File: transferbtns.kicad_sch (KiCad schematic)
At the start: 23 parts, among them J17 8P8C, J18 8P8C, U6 74LS165

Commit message: finish initial schematic design, start pcb layout
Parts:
- J17, J18: footprint (none) -> Phones:AMPHENOL_54602-908LF; DKPN (none) -> 609-1046-ND
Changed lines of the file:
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@@
 			)
 		)
-		(property "Footprint" ""
+		(property "Footprint" "Phones:AMPHENOL_54602-908LF"
 			(at 57.15 76.835 90)
 			(hide yes)
@@
 		)
 		(property "Description" "RJ connector, 8P8C (8 positions 8 connected), RJ31/RJ32/RJ33/RJ34/RJ35/RJ41/RJ45/RJ49/RJ61"
+			(at 57.15 77.47 0)
+			(hide yes)
+			(show_name no)
+			(do_not_autoplace no)
+			(effects
+				(font
+					(size 1.27 1.27)
+				)
+			)
+		)
+		(property "DKPN" "609-1046-ND"
 			(at 57.15 77.47 0)
 			(hide yes)
@@
 		(dnp no)
 		(fields_autoplaced yes)
-		(property "Reference" "#PWR?"
+		(property "Reference" "#PWR0104"
 			(at 85.09 115.57 0)
 			(hide yes)
@@
 			(project "pbx-sniffer-v2"
 				(path "/eb421281-26a1-483f-b39a-0425ec8eb8df/e4c2ebee-8cf8-408f-ab71-48d7afe9e7e1"
-					(reference "#PWR?")
+					(reference "#PWR0104")
 					(unit 1)
 				)
@@
 			)
 		)
-		(property "Footprint" ""
+		(property "Footprint" "Phones:AMPHENOL_54602-908LF"
 			(at 57.15 45.085 90)
 			(hide yes)
@@
 			)
 		)
+		(property "DKPN" "609-1046-ND"
+			(at 57.15 45.72 0)
+			(hide yes)
+			(show_name no)
+			(do_not_autoplace no)
+			(effects
+				(font
+					(size 1.27 1.27)
+				)
+			)
+		)
 		(pin "3"
 		)
@@
 		(dnp no)
 		(fields_autoplaced yes)
-		(property "Reference" "#PWR?"
+		(property "Reference" "#PWR0111"
 			(at 139.7 81.28 0)
 			(hide yes)
@@
 			(project "pbx-sniffer-v2"
 				(path "/eb421281-26a1-483f-b39a-0425ec8eb8df/e4c2ebee-8cf8-408f-ab71-48d7afe9e7e1"
-					(reference "#PWR?")
+					(reference "#PWR0111")
 					(unit 1)
 				)
@@
 		(dnp no)
 		(fields_autoplaced yes)
-		(property "Reference" "#PWR?"
+		(property "Reference" "#PWR0106"
 			(at 85.09 156.21 0)
 			(hide yes)
@@
 			(project "pbx-sniffer-v2"
 				(path "/eb421281-26a1-483f-b39a-0425ec8eb8df/e4c2ebee-8cf8-408f-ab71-48d7afe9e7e1"
-					(reference "#PWR?")
+					(reference "#PWR0106")
 					(unit 1)
 				)
@@
 		(dnp no)
 		(fields_autoplaced yes)
-		(property "Reference" "#PWR?"
+		(property "Reference" "#PWR0110"
 			(at 139.7 25.4 0)
 			(hide yes)
@@
 			(project "pbx-sniffer-v2"
 				(path "/eb421281-26a1-483f-b39a-0425ec8eb8df/e4c2ebee-8cf8-408f-ab71-48d7afe9e7e1"
-					(reference "#PWR?")
+					(reference "#PWR0110")
 					(unit 1)
 				)
@@
 		(dnp no)
 		(fields_autoplaced yes)
-		(property "Reference" "#PWR?"
+		(property "Reference" "#PWR0108"
 			(at 85.09 196.85 0)
 			(hide yes)
@@
 			(project "pbx-sniffer-v2"
 				(path "/eb421281-26a1-483f-b39a-0425ec8eb8df/e4c2ebee-8cf8-408f-ab71-48d7afe9e7e1"
-					(reference "#PWR?")
+					(reference "#PWR0108")
 					(unit 1)
 				)
@@
 		(in_pos_files yes)
 		(dnp no)
-		(property "Reference" "#PWR01"
+		(property "Reference" "#PWR0109"
 			(at 125.73 38.1 0)
 			(hide yes)
@@
 			(project "pbx-sniffer-v2"
 				(path "/eb421281-26a1-483f-b39a-0425ec8eb8df/e4c2ebee-8cf8-408f-ab71-48d7afe9e7e1"
-					(reference "#PWR01")
+					(reference "#PWR0109")
 					(unit 1)
 				)
@@
 		(dnp no)
 		(fields_autoplaced yes)
-		(property "Reference" "#PWR?"
+		(property "Reference" "#PWR0105"
 			(at 85.09 135.89 0)
 			(hide yes)
@@
 			(project "pbx-sniffer-v2"
 				(path "/eb421281-26a1-483f-b39a-0425ec8eb8df/e4c2ebee-8cf8-408f-ab71-48d7afe9e7e1"
-					(reference "#PWR?")
+					(reference "#PWR0105")
 					(unit 1)
 				)
@@
 		(dnp no)
 		(fields_autoplaced yes)
-		(property "Reference" "#PWR?"
+		(property "Reference" "#PWR0103"
 			(at 85.09 95.25 0)
 			(hide yes)
@@
 			(project "pbx-sniffer-v2"
 				(path "/eb421281-26a1-483f-b39a-0425ec8eb8df/e4c2ebee-8cf8-408f-ab71-48d7afe9e7e1"
-					(reference "#PWR?")
+					(reference "#PWR0103")
 					(unit 1)
 				)
@@
 		(dnp no)
 		(fields_autoplaced yes)
-		(property "Reference" "#PWR?"
+		(property "Reference" "#PWR0101"
 			(at 85.09 54.61 0)
 			(hide yes)
@@
 			(project "pbx-sniffer-v2"
 				(path "/eb421281-26a1-483f-b39a-0425ec8eb8df/e4c2ebee-8cf8-408f-ab71-48d7afe9e7e1"
-					(reference "#PWR?")
+					(reference "#PWR0101")
 					(unit 1)
 				)
@@
 		(dnp no)
 		(fields_autoplaced yes)
-		(property "Reference" "#PWR?"
+		(property "Reference" "#PWR0107"
 			(at 85.09 176.53 0)
 			(hide yes)
@@
 			(project "pbx-sniffer-v2"
 				(path "/eb421281-26a1-483f-b39a-0425ec8eb8df/e4c2ebee-8cf8-408f-ab71-48d7afe9e7e1"
-					(reference "#PWR?")
+					(reference "#PWR0107")
 					(unit 1)
 				)
@@
 		(dnp no)
 		(fields_autoplaced yes)
-		(property "Reference" "#PWR010"
+		(property "Reference" "#PWR0100"
 			(at 68.58 69.85 0)
 			(hide yes)
@@
 			(project "pbx-sniffer-v2"
 				(path "/eb421281-26a1-483f-b39a-0425ec8eb8df/e4c2ebee-8cf8-408f-ab71-48d7afe9e7e1"
-					(reference "#PWR010")
+					(reference "#PWR0100")
 					(unit 1)
 				)
@@
 		(dnp no)
 		(fields_autoplaced yes)
-		(property "Reference" "#PWR?"
+		(property "Reference" "#PWR0102"
 			(at 85.09 74.93 0)
 			(hide yes)
@@
 			(project "pbx-sniffer-v2"
 				(path "/eb421281-26a1-483f-b39a-0425ec8eb8df/e4c2ebee-8cf8-408f-ab71-48d7afe9e7e1"
-					(reference "#PWR?")
-					(unit 1)
-				)
+					(reference "#PWR0102")
+					(unit 1)
+				)

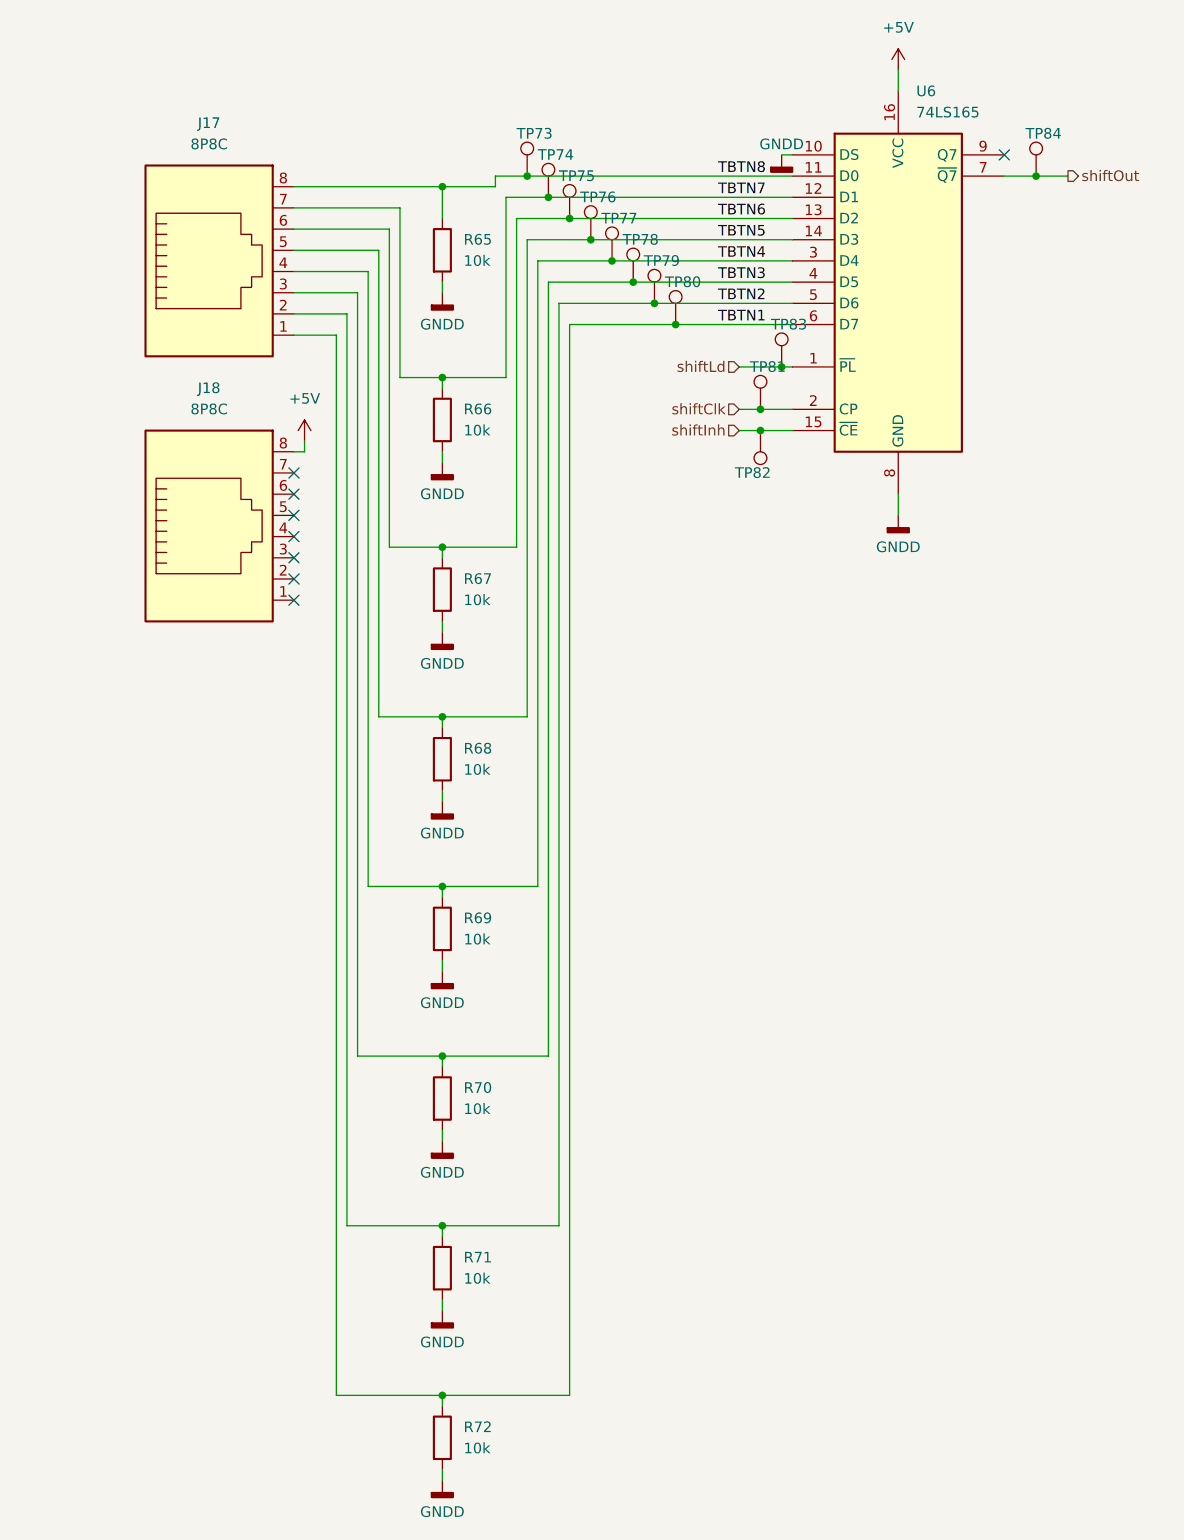
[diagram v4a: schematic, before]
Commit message: place footprints for one line module
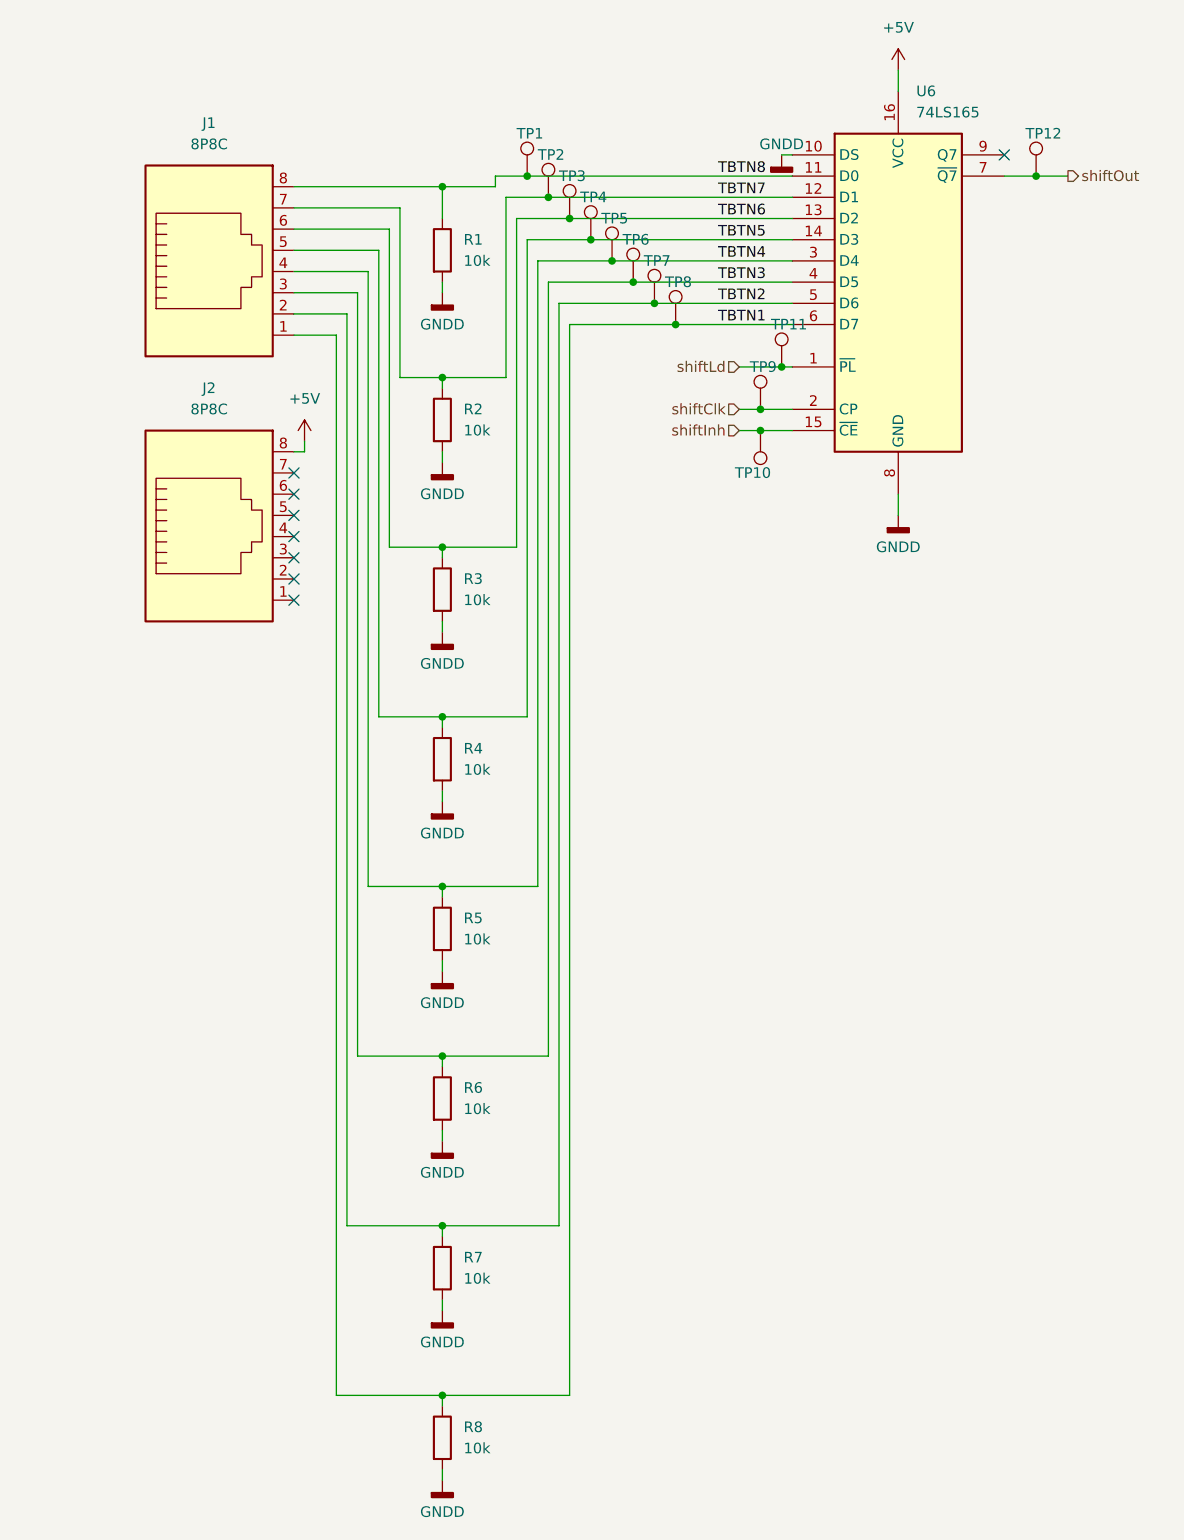
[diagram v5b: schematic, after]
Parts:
- renumbered J17 to J1, J18 to J2, R65 to R1, R66 to R2, R67 to R3, R68 to R4, R69 to R5, R70 to R6, R71 to R7, R72 to R8, TP73 to TP1, TP82 to TP10, TP83 to TP11, TP84 to TP12, TP74 to TP2, TP75 to TP3, TP76 to TP4, TP77 to TP5, TP78 to TP6, TP79 to TP7, TP80 to TP8, TP81 to TP9

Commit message: layout and replicate remaining lines
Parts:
- R1, R2, R3, R4, R5, R6, R7, R8: footprint Resistor_THT:R_Axial_DIN0207_L6.3mm_D2.5mm_P10.16mm_Horizontal -> Resistor_THT:R_Axial_DIN0207_L6.3mm_D2.5mm_P7.62mm_Horizontal
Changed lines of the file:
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@@
 			)
 		)
-		(property "Footprint" "Resistor_THT:R_Axial_DIN0207_L6.3mm_D2.5mm_P10.16mm_Horizontal"
+		(property "Footprint" "Resistor_THT:R_Axial_DIN0207_L6.3mm_D2.5mm_P7.62mm_Horizontal"
 			(at 83.312 124.46 90)
 			(hide yes)
@@
 			)
 		)
-		(property "Footprint" "Resistor_THT:R_Axial_DIN0207_L6.3mm_D2.5mm_P10.16mm_Horizontal"
+		(property "Footprint" "Resistor_THT:R_Axial_DIN0207_L6.3mm_D2.5mm_P7.62mm_Horizontal"
 			(at 83.312 165.1 90)
 			(hide yes)
@@
 			)
 		)
-		(property "Footprint" "Resistor_THT:R_Axial_DIN0207_L6.3mm_D2.5mm_P10.16mm_Horizontal"
+		(property "Footprint" "Resistor_THT:R_Axial_DIN0207_L6.3mm_D2.5mm_P7.62mm_Horizontal"
 			(at 83.312 63.5 90)
 			(hide yes)
@@
 			)
 		)
-		(property "Footprint" "Resistor_THT:R_Axial_DIN0207_L6.3mm_D2.5mm_P10.16mm_Horizontal"
+		(property "Footprint" "Resistor_THT:R_Axial_DIN0207_L6.3mm_D2.5mm_P7.62mm_Horizontal"
 			(at 83.312 144.78 90)
 			(hide yes)
@@
 			)
 		)
-		(property "Footprint" "Resistor_THT:R_Axial_DIN0207_L6.3mm_D2.5mm_P10.16mm_Horizontal"
+		(property "Footprint" "Resistor_THT:R_Axial_DIN0207_L6.3mm_D2.5mm_P7.62mm_Horizontal"
 			(at 83.312 43.18 90)
 			(hide yes)
@@
 			)
 		)
-		(property "Footprint" "Resistor_THT:R_Axial_DIN0207_L6.3mm_D2.5mm_P10.16mm_Horizontal"
+		(property "Footprint" "Resistor_THT:R_Axial_DIN0207_L6.3mm_D2.5mm_P7.62mm_Horizontal"
 			(at 83.312 104.14 90)
 			(hide yes)
@@
 			)
 		)
-		(property "Footprint" "Resistor_THT:R_Axial_DIN0207_L6.3mm_D2.5mm_P10.16mm_Horizontal"
+		(property "Footprint" "Resistor_THT:R_Axial_DIN0207_L6.3mm_D2.5mm_P7.62mm_Horizontal"
 			(at 83.312 83.82 90)
 			(hide yes)
@@
 			)
 		)
-		(property "Footprint" "Resistor_THT:R_Axial_DIN0207_L6.3mm_D2.5mm_P10.16mm_Horizontal"
+		(property "Footprint" "Resistor_THT:R_Axial_DIN0207_L6.3mm_D2.5mm_P7.62mm_Horizontal"
 			(at 83.312 185.42 90)
 			(hide yes)
